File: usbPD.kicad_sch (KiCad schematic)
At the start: 1 part

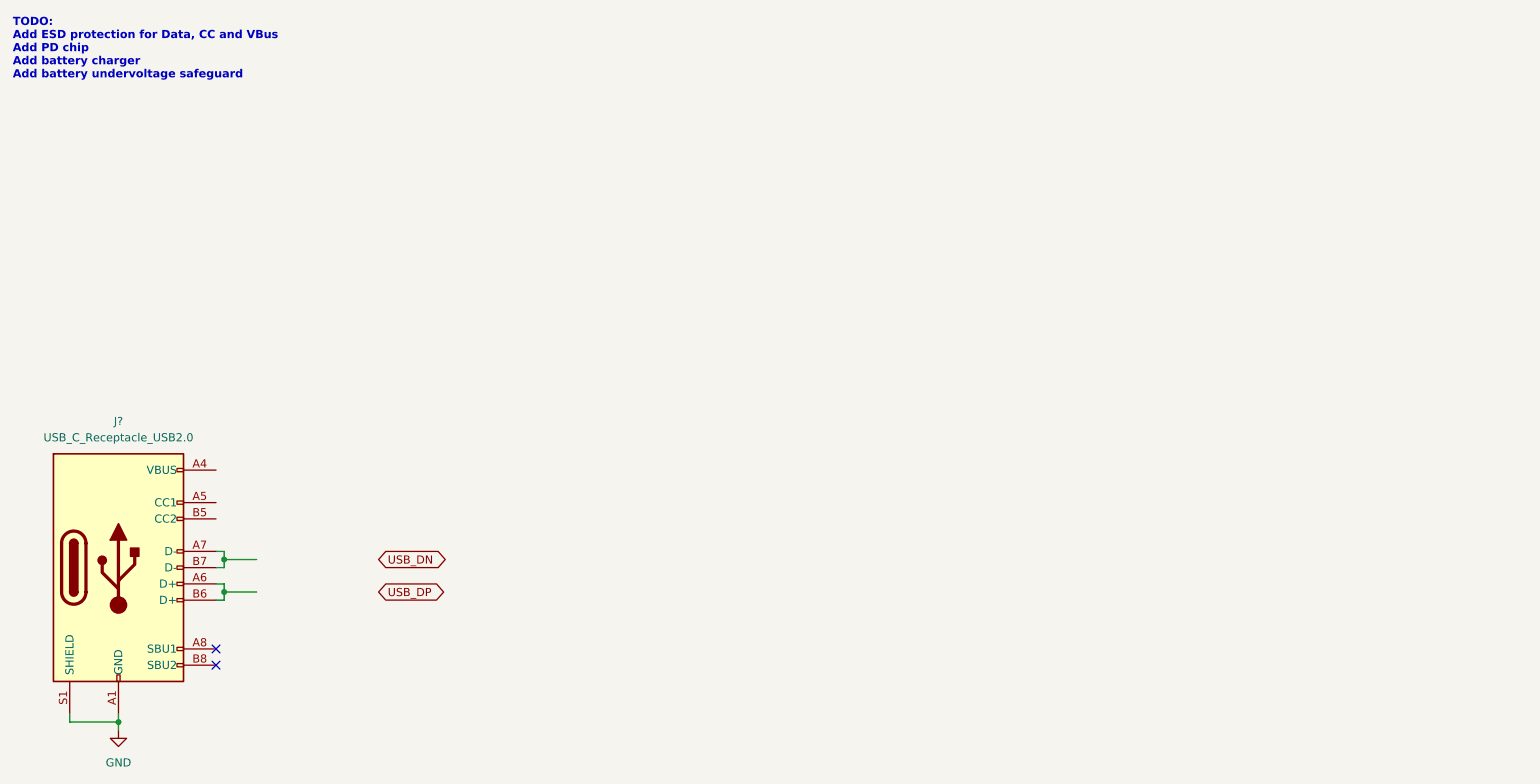
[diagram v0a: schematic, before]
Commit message: Added PD chip with footprint, I2C extension connectors
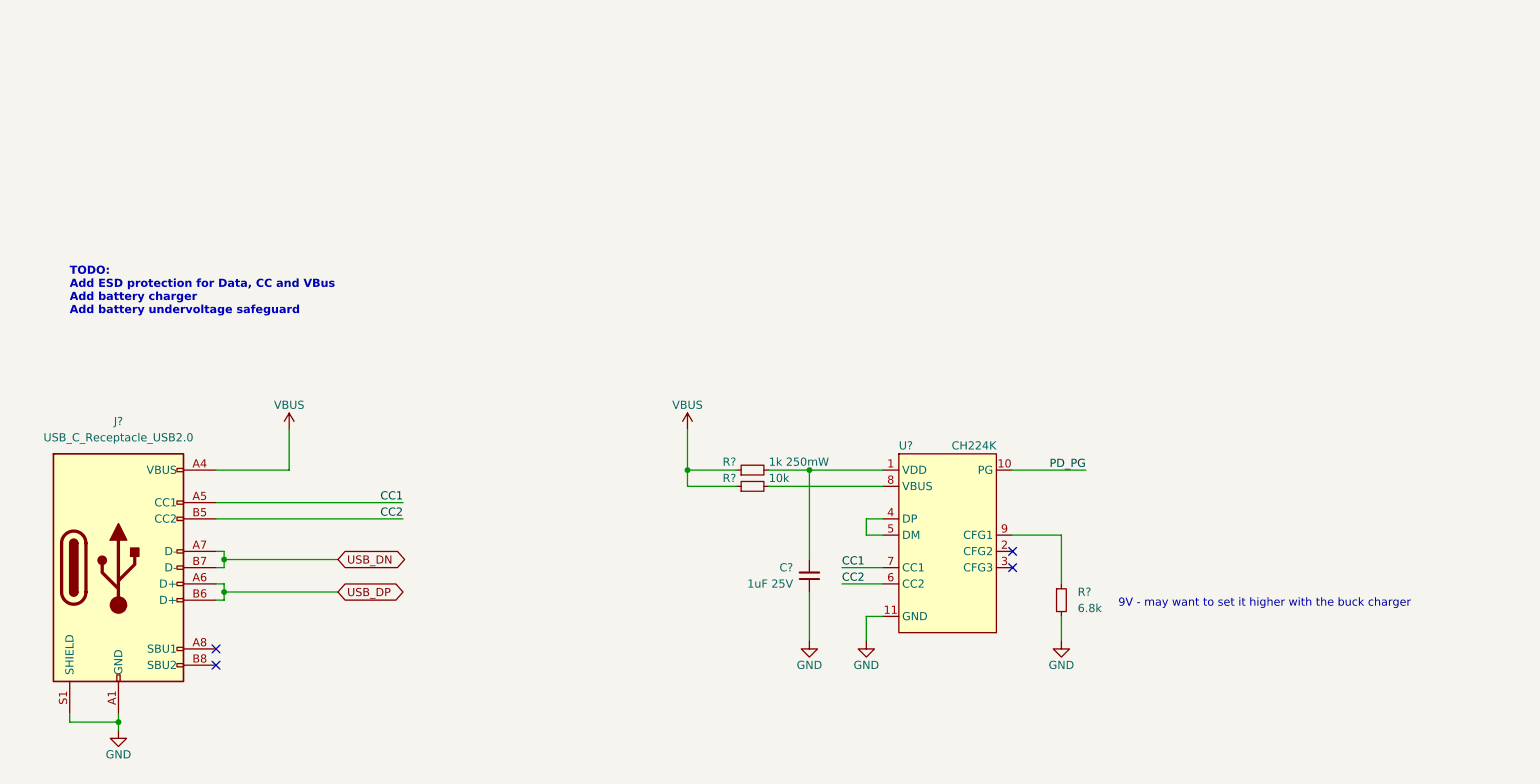
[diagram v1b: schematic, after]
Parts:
- added C?: 1uF 25V, Capacitor_SMD:C_0402_1005Metric, symbol Device:C_Small
- added R?: 10k, Resistor_SMD:R_0402_1005Metric, symbol Device:R_Small
- added R?: 1k 250mW, Resistor_SMD:R_1206_3216Metric, symbol Device:R_Small
- added R?: 6.8k, Resistor_SMD:R_0402_1005Metric, symbol Device:R_Small
- added U?: CH224K, MaxTailsLibrary:ESSOP10, symbol MaxTailsLibrary:CH224K
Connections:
- net GND: now also C?.1, R?.2, U?.11 (GND)
- net USB_DN: now also J?.A7 (D-), J?.B7 (D-)
- net USB_DP: now also J?.A6 (D+), J?.B6 (D+)
- net VBUS: now reaches J?.A4 (VBUS), J?.A9 (VBUS), J?.B4 (VBUS), J?.B9 (VBUS)
- net VBUS: now also R?.1, R?.1
- net CC1: now reaches J?.A5 (CC1)
- net CC1: now also U?.7 (CC1)
- net CC2: now reaches J?.B5 (CC2)
- net CC2: now also U?.6 (CC2)
- new net: R?.2, U?.8 (VBUS)
- new net: C?.2, R?.2, U?.1 (VDD)
- new net: U?.4 (DP), U?.5 (DM)
- new net: R?.1, U?.9 (CFG1)
- new net PD_PG: U?.10 (PG)
- no-connect marks 2 -> 4
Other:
- note added: "9V - may want to set it higher with the buck charger"
- note added: "TODO: Add ESD protection for Data, CC and VBus Add battery charger Add battery undervoltage safeguard"
- note removed: "TODO: Add ESD protection for Data, CC and VBus Add PD chip Add battery charger Add battery undervoltage safeguard"
